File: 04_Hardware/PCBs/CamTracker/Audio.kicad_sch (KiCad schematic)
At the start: 25 parts, among them J27 53047-0210, U1 SC206EEMDA-G51-UGNDA, U13 PAM8302AASCR

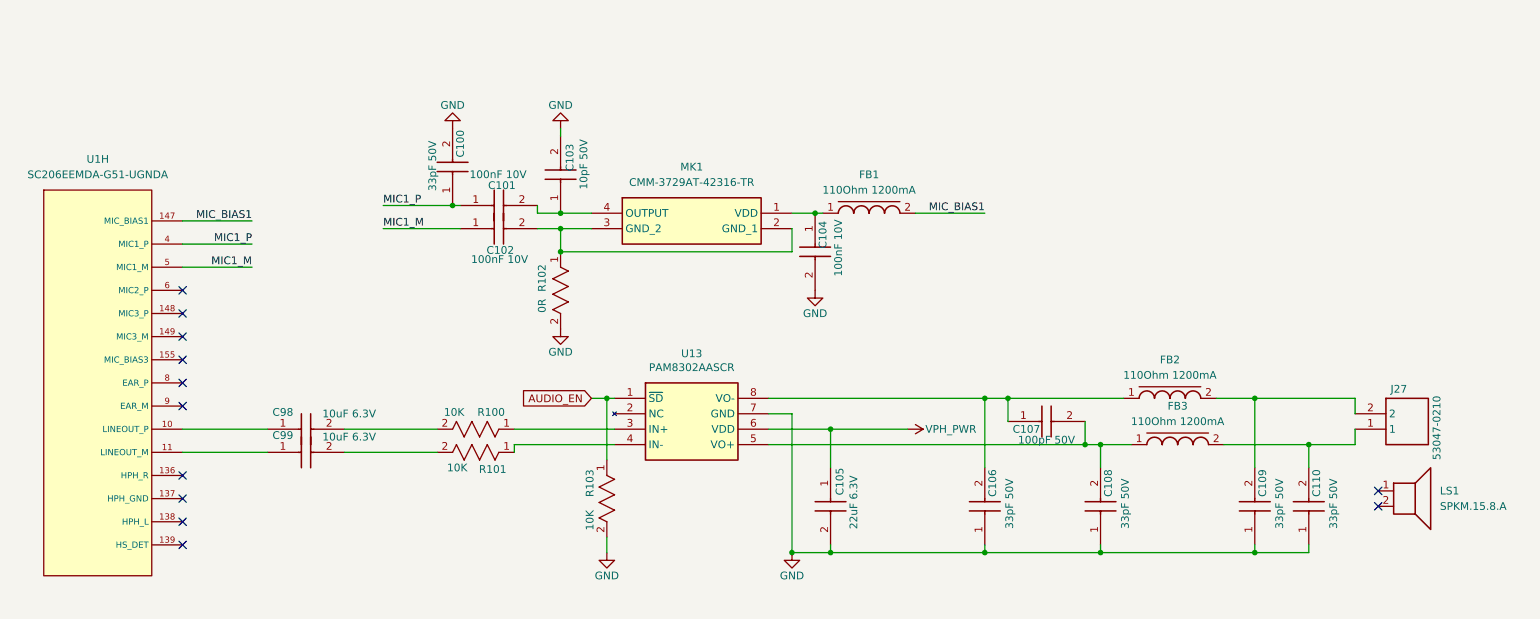
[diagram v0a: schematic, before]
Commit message: feat: Completed Placement v1 in Layout
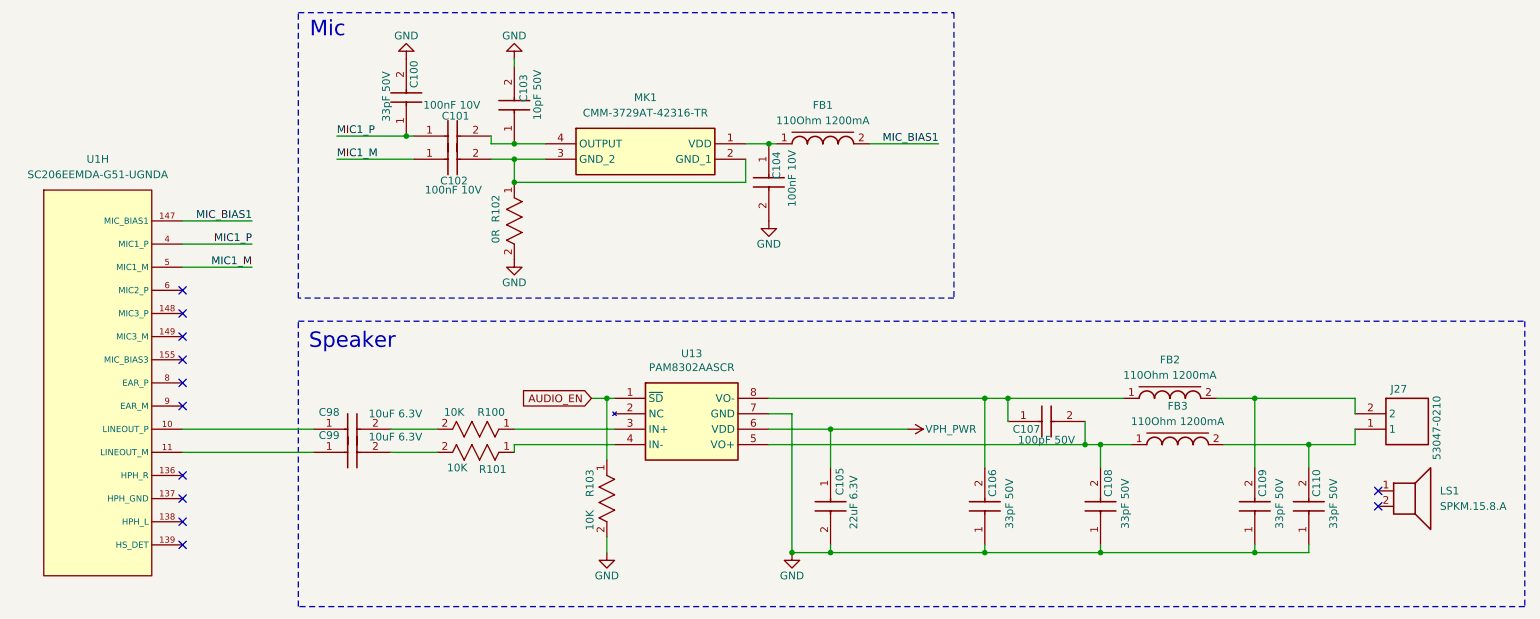
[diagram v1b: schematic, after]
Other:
- note added: "Mic"
- note added: "Speaker"
- moved on the sheet: C100, C101, C102, C103, C104, C98, C99, FB1, MK1, R102

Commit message: feat(PCB): Finalized design and generated Gerber files and BOM
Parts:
- MK1: Part_Number CMM-3729AT-42316-TR -> (none)
